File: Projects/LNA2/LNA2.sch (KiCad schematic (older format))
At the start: 9 parts, among them J1 SMA-J-P-H-ST-EM1, J2 SMA-J-P-H-ST-EM1, U1 TRF37A73

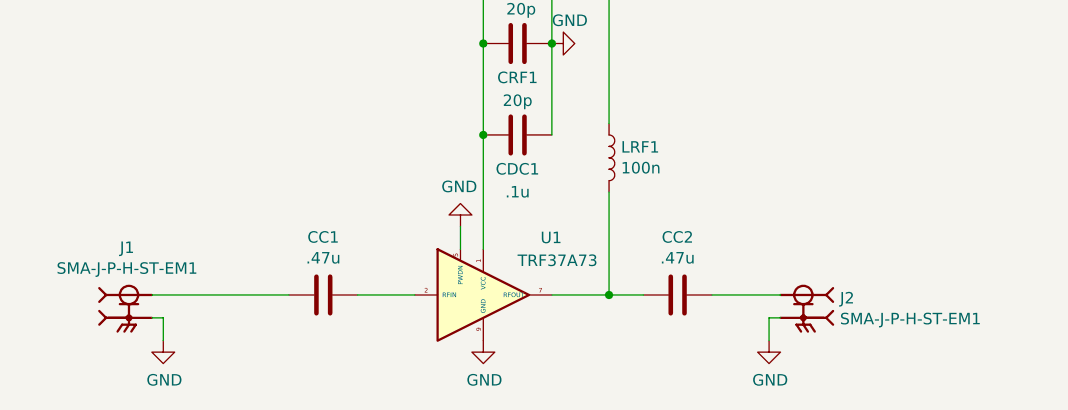
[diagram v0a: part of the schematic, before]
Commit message: fixed SMA connectors
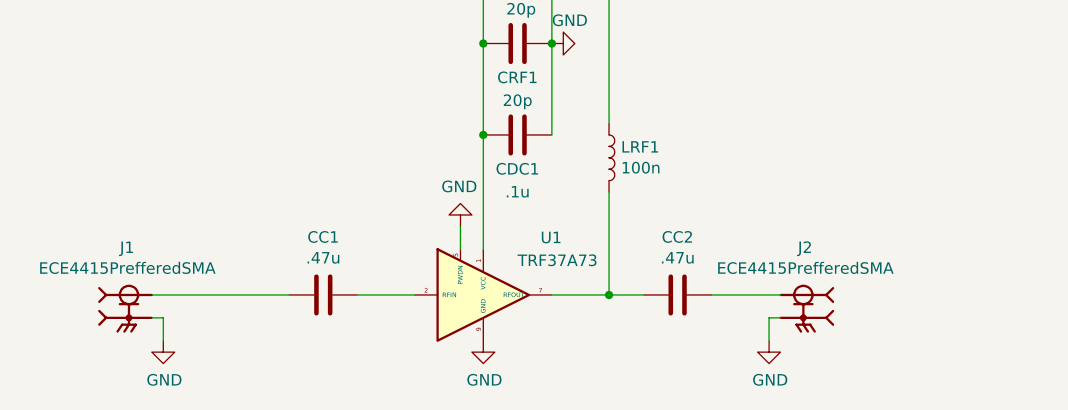
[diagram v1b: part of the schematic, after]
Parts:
- removed J1, J2: SMA-J-P-H-ST-EM1, SAMTEC_SMA-J-P-H-ST-EM1, symbol RandomSMAIFoundOnline:SMA-J-P-H-ST-EM1
- added J1, J2: ECE4415PrefferedSMA, AdditionalLibs:ECE4415PrefferedSMA, symbol AdditionalParts:ECE4415PrefferedSMA
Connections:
- net GND: now also J1.S1, J1.S2, J1.S3, J1.S4, J2.S1, J2.S2, J2.S3, J2.S4
- net at CC1.2: now also J1.1
- net at CC2.1: now also J2.1
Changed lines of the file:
@@
 	5450 1450 5450 1600
 $Comp
-L RandomSMAIFoundOnline:SMA-J-P-H-ST-EM1 J1
-U 1 1 6009B200
-P 3900 3200
-F 0 "J1" H 3892 3507 50  0000 C CNN
-F 1 "SMA-J-P-H-ST-EM1" H 3892 3416 50  0000 C CNN
-F 2 "SAMTEC_SMA-J-P-H-ST-EM1" H 3900 3200 50  0001 L BNN
-F 3 "" H 3900 3200 50  0001 L BNN
-F 4 "Samtec" H 3900 3200 50  0001 L BNN "MANUFACTURER"
-F 5 "G" H 3900 3200 50  0001 L BNN "PARTREV"
-F 6 "Manufacturer Recommendations" H 3900 3200 50  0001 L BNN "STANDARD"
-F 7 "3.675mm" H 3900 3200 50  0001 L BNN "MAXIMUM_PACKAGE_HEIGHT"
-	1    3900 3200
-	1    0    0    -1
-$EndComp
-$Comp
-L power:GND #PWR?
+L power:GND #PWR0101
 U 1 1 6009D84E
 P 4050 3300
-F 0 "#PWR?" H 4050 3050 50  0001 C CNN
+F 0 "#PWR0101" H 4050 3050 50  0001 C CNN
 F 1 "GND" H 4055 3127 50  0000 C CNN
 F 2 "" H 4050 3300 50  0001 C CNN
@@
 	4000 3100 4600 3100
 $Comp
-L RandomSMAIFoundOnline:SMA-J-P-H-ST-EM1 J2
-U 1 1 6009E796
-P 6850 3200
-F 0 "J2" H 6690 3286 50  0000 R CNN
-F 1 "SMA-J-P-H-ST-EM1" H 6690 3195 50  0000 R CNN
-F 2 "SAMTEC_SMA-J-P-H-ST-EM1" H 6850 3200 50  0001 L BNN
-F 3 "" H 6850 3200 50  0001 L BNN
-F 4 "Samtec" H 6850 3200 50  0001 L BNN "MANUFACTURER"
-F 5 "G" H 6850 3200 50  0001 L BNN "PARTREV"
-F 6 "Manufacturer Recommendations" H 6850 3200 50  0001 L BNN "STANDARD"
-F 7 "3.675mm" H 6850 3200 50  0001 L BNN "MAXIMUM_PACKAGE_HEIGHT"
-	1    6850 3200
-	-1   0    0    -1
-$EndComp
-$Comp
-L power:GND #PWR?
+L power:GND #PWR0106
 U 1 1 600A4C90
 P 6700 3300
-F 0 "#PWR?" H 6700 3050 50  0001 C CNN
+F 0 "#PWR0106" H 6700 3050 50  0001 C CNN
 F 1 "GND" H 6705 3127 50  0000 C CNN
 F 2 "" H 6700 3300 50  0001 C CNN
@@
 Wire Wire Line
 	6700 3200 6750 3200
+$Comp
+L AdditionalParts:ECE4415PrefferedSMA J1
+U 1 1 600F5A9E
+P 3900 3200
+F 0 "J1" H 3892 3507 50  0000 C CNN
+F 1 "ECE4415PrefferedSMA" H 3892 3416 50  0000 C CNN
+F 2 "AdditionalLibs:ECE4415PrefferedSMA" H 3900 3200 50  0001 L BNN
+F 3 "" H 3900 3200 50  0001 L BNN
+F 4 "Manufacturer Recommendations" H 3900 3200 50  0001 L BNN "STANDARD"
+F 5 "8.052 mm" H 3900 3200 50  0001 L BNN "MAXIMUM_PACKAGE_HEIGHT"
+F 6 "Cinch Connectivity" H 3900 3200 50  0001 L BNN "MANUFACTURER"
+F 7 "5" H 3900 3200 50  0001 L BNN "PARTREV"
+	1    3900 3200
+	1    0    0    -1
+$EndComp
+$Comp
+L AdditionalParts:ECE4415PrefferedSMA J2
+U 1 1 600FBB2C
+P 6850 3200
+F 0 "J2" H 6842 3507 50  0000 C CNN
+F 1 "ECE4415PrefferedSMA" H 6842 3416 50  0000 C CNN
+F 2 "AdditionalLibs:ECE4415PrefferedSMA" H 6850 3200 50  0001 L BNN
+F 3 "" H 6850 3200 50  0001 L BNN
+F 4 "Manufacturer Recommendations" H 6850 3200 50  0001 L BNN "STANDARD"
+F 5 "8.052 mm" H 6850 3200 50  0001 L BNN "MAXIMUM_PACKAGE_HEIGHT"
+F 6 "Cinch Connectivity" H 6850 3200 50  0001 L BNN "MANUFACTURER"
+F 7 "5" H 6850 3200 50  0001 L BNN "PARTREV"
+	1    6850 3200
+	-1   0    0    -1
+$EndComp
 $EndSCHEMATC

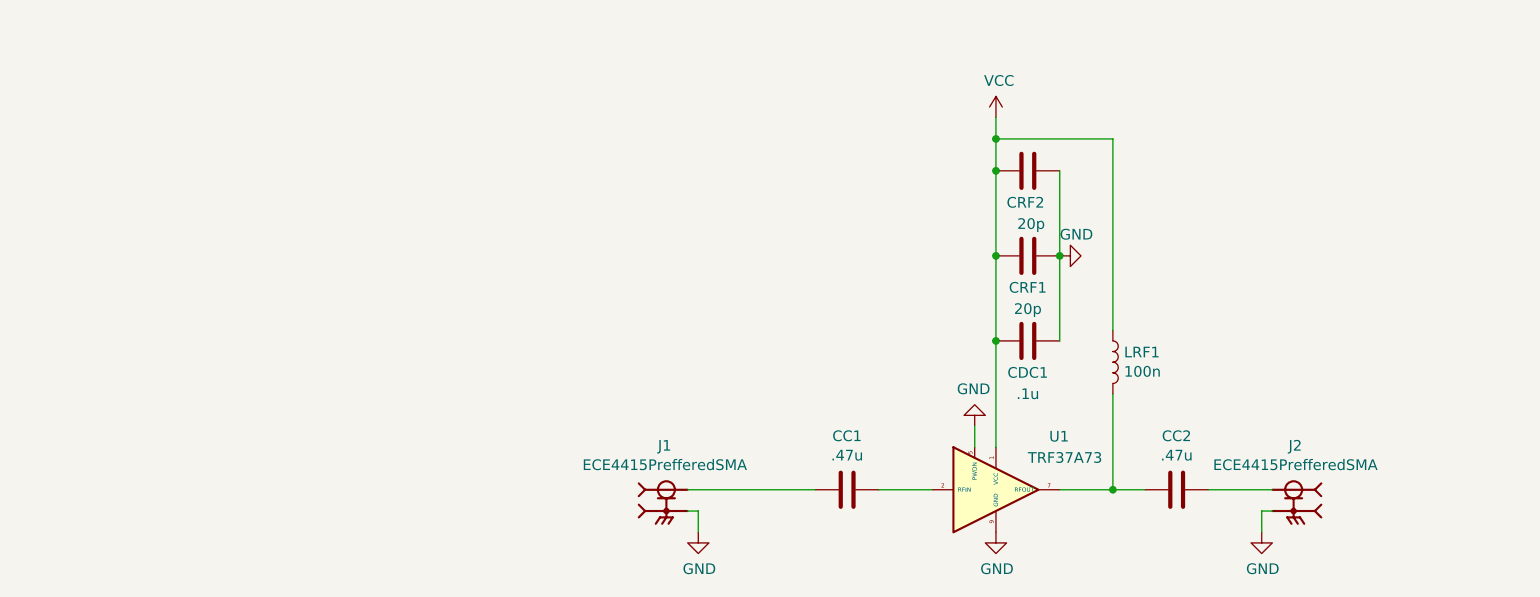
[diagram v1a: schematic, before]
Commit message: added via stitching to the boards and changed to a barrel jack on the LNA
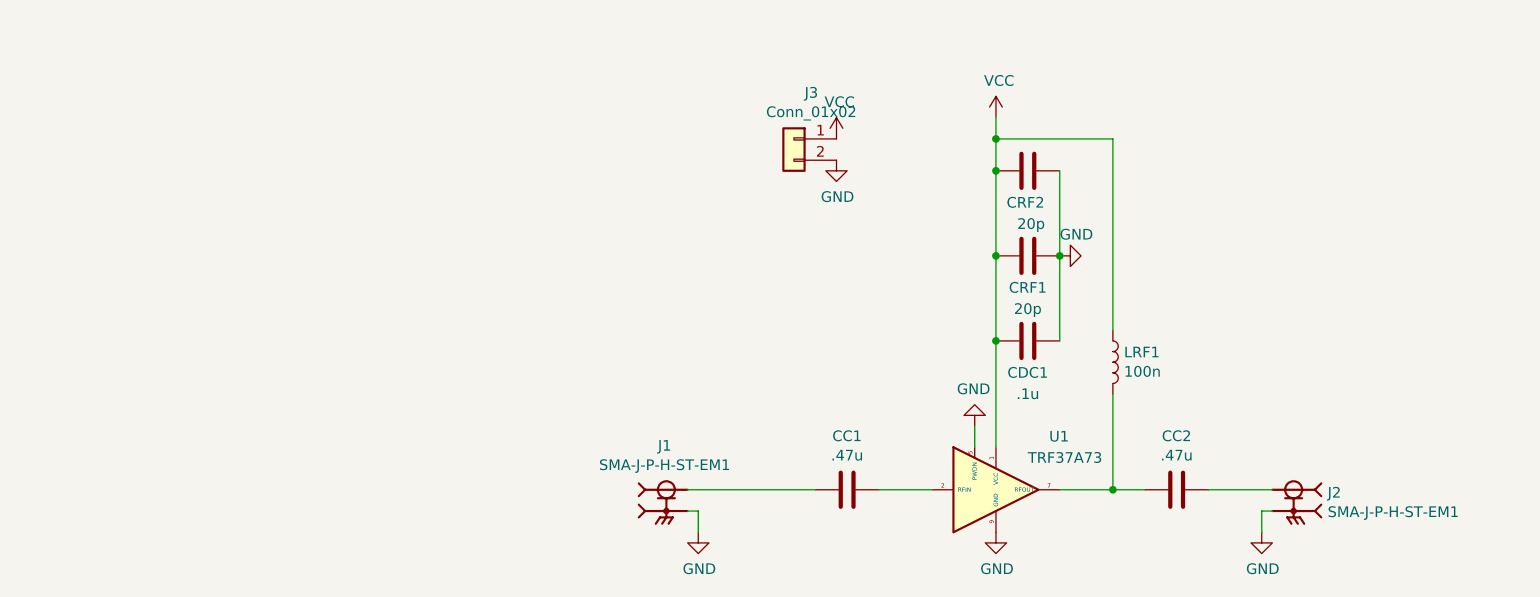
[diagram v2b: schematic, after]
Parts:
- removed J1, J2: ECE4415PrefferedSMA, AdditionalLibs:ECE4415PrefferedSMA, symbol AdditionalParts:ECE4415PrefferedSMA
- added J1, J2: SMA-J-P-H-ST-EM1, SAMTEC_SMA-J-P-H-ST-EM1, symbol RandomSMAIFoundOnline:SMA-J-P-H-ST-EM1
- added J3: Conn_01x02, Connector_PinHeader_2.54mm:PinHeader_1x02_P2.54mm_Vertical, symbol Connector_Generic:Conn_01x02
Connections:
- net GND: now also J1.2_1, J1.2_2, J1.3_1, J1.3_2, J2.2_1, J2.2_2, J2.3_1, J2.3_2, J3.2 (Pin_2)
- net VCC: now also J3.1 (Pin_1)
- net at CC1.2: now also J1.1
- net at CC2.1: now also J2.1
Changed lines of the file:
@@
 	6700 3200 6750 3200
 $Comp
-L AdditionalParts:ECE4415PrefferedSMA J1
-U 1 1 600F5A9E
+L Connector_Generic:Conn_01x02 J3
+U 1 1 60106FBE
+P 4500 1450
+F 0 "J3" H 4418 1667 50  0000 C CNN
+F 1 "Conn_01x02" H 4418 1576 50  0000 C CNN
+F 2 "Connector_PinHeader_2.54mm:PinHeader_1x02_P2.54mm_Vertical" H 4500 1450 50  0001 C CNN
+F 3 "~" H 4500 1450 50  0001 C CNN
+	1    4500 1450
+	-1   0    0    -1
+$EndComp
+$Comp
+L power:VCC #PWR?
+U 1 1 6010742C
+P 4700 1450
+F 0 "#PWR?" H 4700 1300 50  0001 C CNN
+F 1 "VCC" H 4715 1623 50  0000 C CNN
+F 2 "" H 4700 1450 50  0001 C CNN
+F 3 "" H 4700 1450 50  0001 C CNN
+	1    4700 1450
+	1    0    0    -1
+$EndComp
+$Comp
+L power:GND #PWR?
+U 1 1 6010771D
+P 4700 1550
+F 0 "#PWR?" H 4700 1300 50  0001 C CNN
+F 1 "GND" H 4705 1377 50  0000 C CNN
+F 2 "" H 4700 1550 50  0001 C CNN
+F 3 "" H 4700 1550 50  0001 C CNN
+	1    4700 1550
+	1    0    0    -1
+$EndComp
+$Comp
+L RandomSMAIFoundOnline:SMA-J-P-H-ST-EM1 J1
+U 1 1 60104F62
 P 3900 3200
 F 0 "J1" H 3892 3507 50  0000 C CNN
-F 1 "ECE4415PrefferedSMA" H 3892 3416 50  0000 C CNN
-F 2 "AdditionalLibs:ECE4415PrefferedSMA" H 3900 3200 50  0001 L BNN
+F 1 "SMA-J-P-H-ST-EM1" H 3892 3416 50  0000 C CNN
+F 2 "SAMTEC_SMA-J-P-H-ST-EM1" H 3900 3200 50  0001 L BNN
 F 3 "" H 3900 3200 50  0001 L BNN
-F 4 "Manufacturer Recommendations" H 3900 3200 50  0001 L BNN "STANDARD"
-F 5 "8.052 mm" H 3900 3200 50  0001 L BNN "MAXIMUM_PACKAGE_HEIGHT"
-F 6 "Cinch Connectivity" H 3900 3200 50  0001 L BNN "MANUFACTURER"
-F 7 "5" H 3900 3200 50  0001 L BNN "PARTREV"
+F 4 "Samtec" H 3900 3200 50  0001 L BNN "MANUFACTURER"
+F 5 "G" H 3900 3200 50  0001 L BNN "PARTREV"
+F 6 "Manufacturer Recommendations" H 3900 3200 50  0001 L BNN "STANDARD"
+F 7 "3.675mm" H 3900 3200 50  0001 L BNN "MAXIMUM_PACKAGE_HEIGHT"
 	1    3900 3200
 	1    0    0    -1
 $EndComp
 $Comp
-L AdditionalParts:ECE4415PrefferedSMA J2
-U 1 1 600FBB2C
+L RandomSMAIFoundOnline:SMA-J-P-H-ST-EM1 J2
+U 1 1 60106D72
 P 6850 3200
-F 0 "J2" H 6842 3507 50  0000 C CNN
-F 1 "ECE4415PrefferedSMA" H 6842 3416 50  0000 C CNN
-F 2 "AdditionalLibs:ECE4415PrefferedSMA" H 6850 3200 50  0001 L BNN
+F 0 "J2" H 6690 3286 50  0000 R CNN
+F 1 "SMA-J-P-H-ST-EM1" H 6690 3195 50  0000 R CNN
+F 2 "SAMTEC_SMA-J-P-H-ST-EM1" H 6850 3200 50  0001 L BNN
 F 3 "" H 6850 3200 50  0001 L BNN
-F 4 "Manufacturer Recommendations" H 6850 3200 50  0001 L BNN "STANDARD"
-F 5 "8.052 mm" H 6850 3200 50  0001 L BNN "MAXIMUM_PACKAGE_HEIGHT"
-F 6 "Cinch Connectivity" H 6850 3200 50  0001 L BNN "MANUFACTURER"
-F 7 "5" H 6850 3200 50  0001 L BNN "PARTREV"
+F 4 "Samtec" H 6850 3200 50  0001 L BNN "MANUFACTURER"
+F 5 "G" H 6850 3200 50  0001 L BNN "PARTREV"
+F 6 "Manufacturer Recommendations" H 6850 3200 50  0001 L BNN "STANDARD"
+F 7 "3.675mm" H 6850 3200 50  0001 L BNN "MAXIMUM_PACKAGE_HEIGHT"
 	1    6850 3200
 	-1   0    0    -1

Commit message: added linear reg to the rf gain block
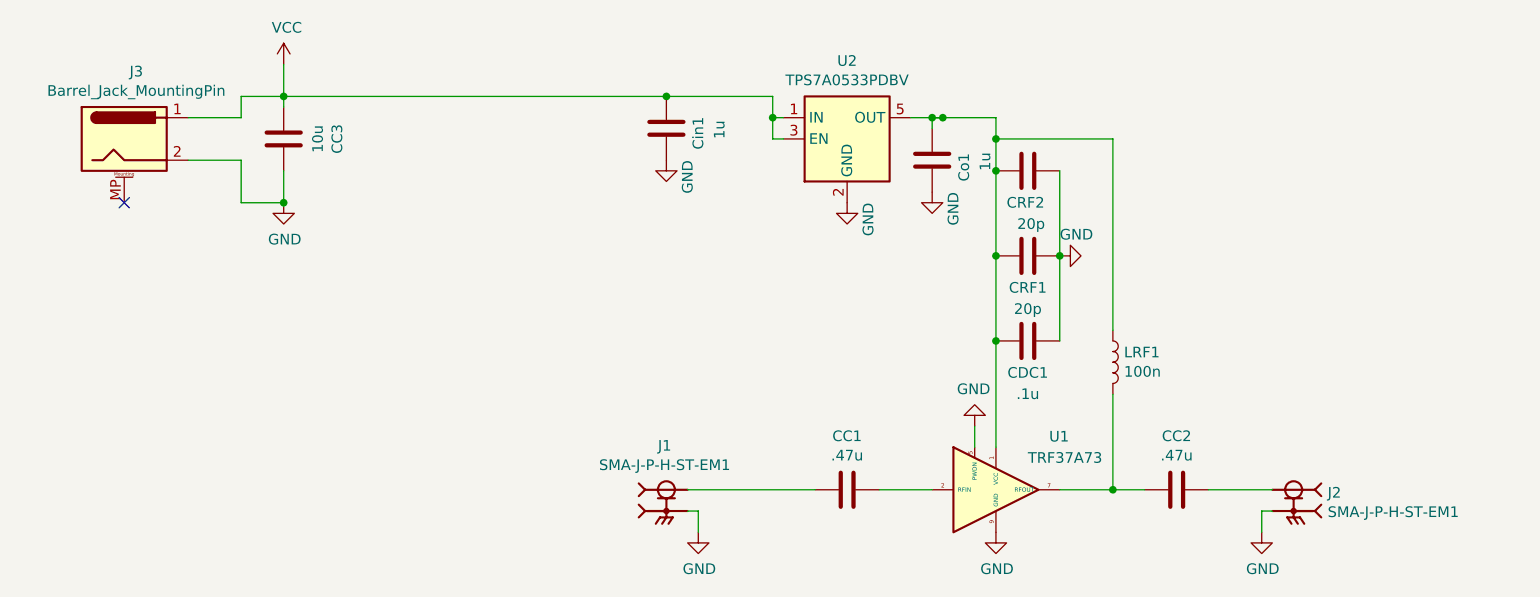
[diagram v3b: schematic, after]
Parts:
- removed J3: Conn_01x02, Connector_PinHeader_2.54mm:PinHeader_1x02_P2.54mm_Vertical, symbol Connector_Generic:Conn_01x02
- added CC3: 10u, Capacitor_SMD:C_0805_2012Metric, symbol Device:C
- added Cin1, Co1: 1u, Capacitor_SMD:C_0805_2012Metric, symbol Device:C
- added J3: Barrel_Jack_MountingPin, Connector_BarrelJack:BarrelJack_Horizontal, symbol Connector:Barrel_Jack_MountingPin
- added U2: TPS7A0533PDBV, Package_TO_SOT_SMD:SOT-23-5, symbol Regulator_Linear:TPS7A0533PDBV
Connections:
- net GND: now also CC3.1, Cin1.1, Co1.1, J3.2, U2.2 (GND)
- net VCC: now also CC3.2, Cin1.2, J3.1, U2.1 (IN), U2.3 (EN); no longer CDC1.1, CRF1.1, CRF2.1, LRF1.1, U1.1 (VCC)
- new net: CDC1.1, CRF1.1, CRF2.1, Co1.2, LRF1.1, U1.1 (VCC), U2.5 (OUT)
- no-connect marks 0 -> 1
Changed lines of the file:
@@
 	5350 2900 5350 2800
-$Comp
-L power:VCC #PWR0103
-U 1 1 6007D5C0
-P 5450 1350
-F 0 "#PWR0103" H 5450 1200 50  0001 C CNN
-F 1 "VCC" H 5465 1523 50  0000 C CNN
-F 2 "" H 5450 1350 50  0001 C CNN
-F 3 "" H 5450 1350 50  0001 C CNN
-	1    5450 1350
-	1    0    0    -1
-$EndComp
 $Comp
 L power:GND #PWR0104
@@
 Wire Wire Line
 	6700 3200 6750 3200
-$Comp
-L Connector_Generic:Conn_01x02 J3
-U 1 1 60106FBE
-P 4500 1450
-F 0 "J3" H 4418 1667 50  0000 C CNN
-F 1 "Conn_01x02" H 4418 1576 50  0000 C CNN
-F 2 "Connector_PinHeader_2.54mm:PinHeader_1x02_P2.54mm_Vertical" H 4500 1450 50  0001 C CNN
-F 3 "~" H 4500 1450 50  0001 C CNN
-	1    4500 1450
-	-1   0    0    -1
-$EndComp
-$Comp
-L power:VCC #PWR?
-U 1 1 6010742C
-P 4700 1450
-F 0 "#PWR?" H 4700 1300 50  0001 C CNN
-F 1 "VCC" H 4715 1623 50  0000 C CNN
-F 2 "" H 4700 1450 50  0001 C CNN
-F 3 "" H 4700 1450 50  0001 C CNN
-	1    4700 1450
-	1    0    0    -1
-$EndComp
-$Comp
-L power:GND #PWR?
-U 1 1 6010771D
-P 4700 1550
-F 0 "#PWR?" H 4700 1300 50  0001 C CNN
-F 1 "GND" H 4705 1377 50  0000 C CNN
-F 2 "" H 4700 1550 50  0001 C CNN
-F 3 "" H 4700 1550 50  0001 C CNN
-	1    4700 1550
-	1    0    0    -1
-$EndComp
 $Comp
 L RandomSMAIFoundOnline:SMA-J-P-H-ST-EM1 J1
@@
 	-1   0    0    -1
 $EndComp
+$Comp
+L Connector:Barrel_Jack_MountingPin J3
+U 1 1 6010B5E5
+P 1350 1450
+F 0 "J3" H 1407 1767 50  0000 C CNN
+F 1 "Barrel_Jack_MountingPin" H 1407 1676 50  0000 C CNN
+F 2 "Connector_BarrelJack:BarrelJack_Horizontal" H 1400 1410 50  0001 C CNN
+F 3 "~" H 1400 1410 50  0001 C CNN
+	1    1350 1450
+	1    0    0    -1
+$EndComp
+NoConn ~ 1350 1750
+$Comp
+L power:VCC #PWR0107
+U 1 1 6010C0C3
+P 2100 1100
+F 0 "#PWR0107" H 2100 950 50  0001 C CNN
+F 1 "VCC" H 2115 1273 50  0000 C CNN
+F 2 "" H 2100 1100 50  0001 C CNN
+F 3 "" H 2100 1100 50  0001 C CNN
+	1    2100 1100
+	1    0    0    -1
+$EndComp
+$Comp
+L Device:C CC3
+U 1 1 6010D31A
+P 2100 1450
+F 0 "CC3" V 1848 1450 50  0000 C CNN
+F 1 "10u" V 1939 1450 50  0000 C CNN
+F 2 "Capacitor_SMD:C_0805_2012Metric" H 2138 1300 50  0001 C CNN
+F 3 "~" H 2100 1450 50  0001 C CNN
+	1    2100 1450
+	-1   0    0    1
+$EndComp
+Wire Wire Line
+	1650 1350 1900 1350
+Wire Wire Line
+	1900 1350 1900 1250
+Wire Wire Line
+	1900 1250 2100 1250
+Wire Wire Line
+	2100 1250 2100 1300
+Wire Wire Line
+	2100 1100 2100 1250
+Connection ~ 2100 1250
+Wire Wire Line
+	1900 1550 1900 1750
+Wire Wire Line
+	1900 1750 2100 1750
+Wire Wire Line
+	2100 1750 2100 1600
+Wire Wire Line
+	1650 1550 1900 1550
+$Comp
+L power:GND #PWR0108
+U 1 1 6010F8E1
+P 2100 1750
+F 0 "#PWR0108" H 2100 1500 50  0001 C CNN
+F 1 "GND" H 2105 1577 50  0000 C CNN
+F 2 "" H 2100 1750 50  0001 C CNN
+F 3 "" H 2100 1750 50  0001 C CNN
+	1    2100 1750
+	1    0    0    -1
+$EndComp
+Connection ~ 2100 1750
+$Comp
+L Regulator_Linear:TPS7A0533PDBV U2
+U 1 1 601160D3
+P 4750 1450
+F 0 "U2" H 4750 1817 50  0000 C CNN
+F 1 "TPS7A0533PDBV" H 4750 1726 50  0000 C CNN
+F 2 "Package_TO_SOT_SMD:SOT-23-5" H 4750 1800 50  0001 C CNN
+F 3 "https://www.ti.com/lit/ds/symlink/tps7a05.pdf" H 4750 1950 50  0001 C CNN
+	1    4750 1450
+	1    0    0    -1
+$EndComp
+$Comp
+L Device:C Co1
+U 1 1 6011F8A9
+P 5150 1550
+F 0 "Co1" V 5000 1650 50  0000 R CNN
+F 1 "1u" V 4900 1600 50  0000 R CNN
+F 2 "Capacitor_SMD:C_0805_2012Metric" H 5188 1400 50  0001 C CNN
+F 3 "~" H 5150 1550 50  0001 C CNN
+	1    5150 1550
+	-1   0    0    1
+$EndComp
+Wire Wire Line
+	5050 1350 5150 1350
+Wire Wire Line
+	5150 1350 5150 1400
+$Comp
+L power:GND #PWR0103
+U 1 1 601205FC
+P 5150 1700
+F 0 "#PWR0103" H 5150 1450 50  0001 C CNN
+F 1 "GND" V 5250 1700 50  0000 R CNN
+F 2 "" H 5150 1700 50  0001 C CNN
+F 3 "" H 5150 1700 50  0001 C CNN
+	1    5150 1700
+	1    0    0    -1
+$EndComp
+$Comp
+L power:GND #PWR0109
+U 1 1 60120B3E
+P 4750 1750
+F 0 "#PWR0109" H 4750 1500 50  0001 C CNN
+F 1 "GND" V 4850 1750 50  0000 R CNN
+F 2 "" H 4750 1750 50  0001 C CNN
+F 3 "" H 4750 1750 50  0001 C CNN
+	1    4750 1750
+	1    0    0    -1
+$EndComp
+Wire Wire Line
+	4450 1350 4400 1350
+Wire Wire Line
+	4400 1350 4400 1450
+Wire Wire Line
+	4400 1450 4450 1450
+Wire Wire Line
+	2100 1250 3900 1250
+Wire Wire Line
+	4400 1250 4400 1350
+Connection ~ 4400 1350
+$Comp
+L Device:C Cin1
+U 1 1 60121EE9
+P 3900 1400
+F 0 "Cin1" V 3750 1500 50  0000 R CNN
+F 1 "1u" V 3650 1450 50  0000 R CNN
+F 2 "Capacitor_SMD:C_0805_2012Metric" H 3938 1250 50  0001 C CNN
+F 3 "~" H 3900 1400 50  0001 C CNN
+	1    3900 1400
+	-1   0    0    1
+$EndComp
+Connection ~ 3900 1250
+Wire Wire Line
+	3900 1250 4400 1250
+$Comp
+L power:GND #PWR0110
+U 1 1 60122107
+P 3900 1550
+F 0 "#PWR0110" H 3900 1300 50  0001 C CNN
+F 1 "GND" V 4000 1550 50  0000 R CNN
+F 2 "" H 3900 1550 50  0001 C CNN
+F 3 "" H 3900 1550 50  0001 C CNN
+	1    3900 1550
+	1    0    0    -1
+$EndComp
+Connection ~ 5150 1350
+Connection ~ 5200 1350
+Wire Wire Line
+	5200 1350 5150 1350
+Wire Wire Line
+	5150 1350 5450 1350
 $EndSCHEMATC
